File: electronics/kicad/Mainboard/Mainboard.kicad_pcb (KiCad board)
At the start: 2 copper layers, 99 x 53 mm, 30 parts, among them J1 GND Pair, J10 Conn_01x05, J11 Box Switch 1, J12 Box Switch 2, J13 Bos Switch 3, J14 LED Strip, J2 X-Axis Hall, J3 Y-Axis Hall, J4 Conn_01x05, J5 Conn_01x05, J6 USB_A_Stacked, J7 Conn_01x05, J8 Conn_01x05, J9 Conn_01x05, M2.5 MountingHole_2.7mm_M2.5_DIN96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, U1 ESP32-C6-DevKitC-1, U2 MCP23017_SP

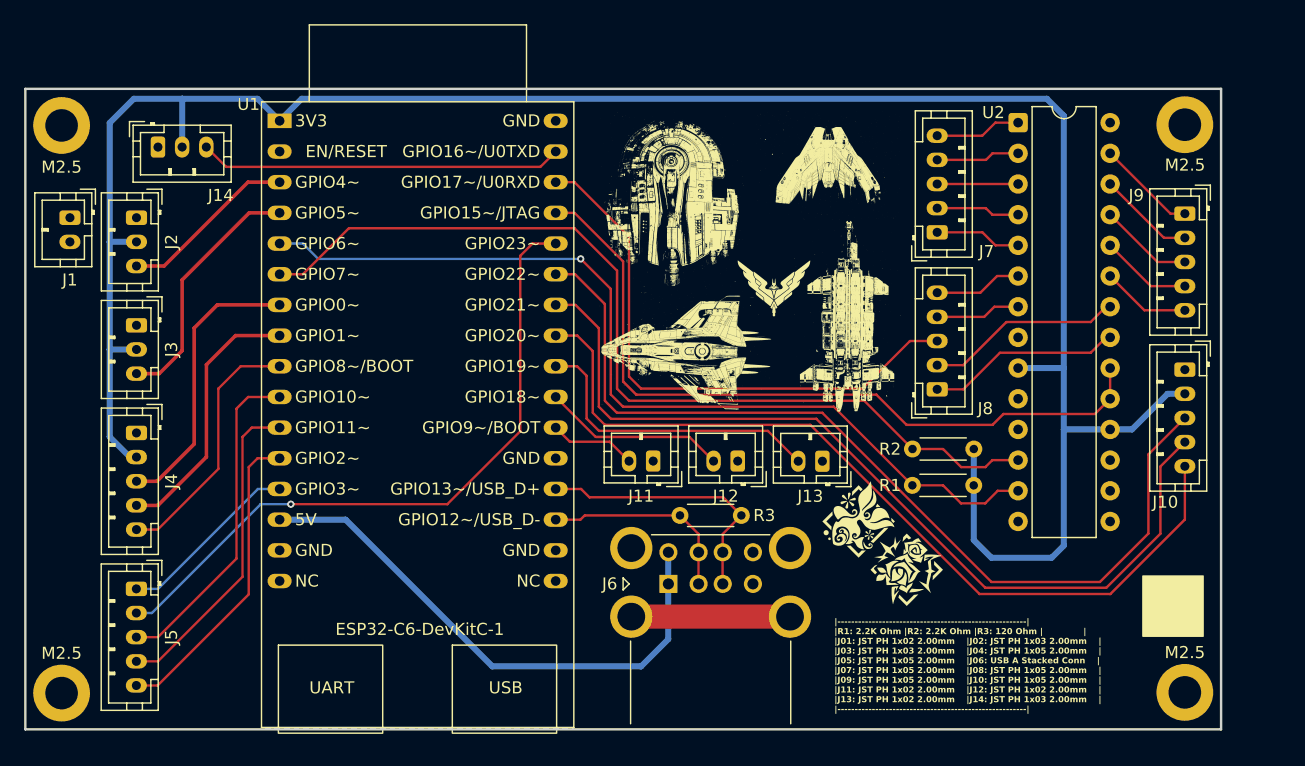
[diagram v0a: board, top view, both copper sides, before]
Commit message: Updated Schematic
Some Parts were replaced with Hand Solder SMD components where possible. Routing changed to work with new parts
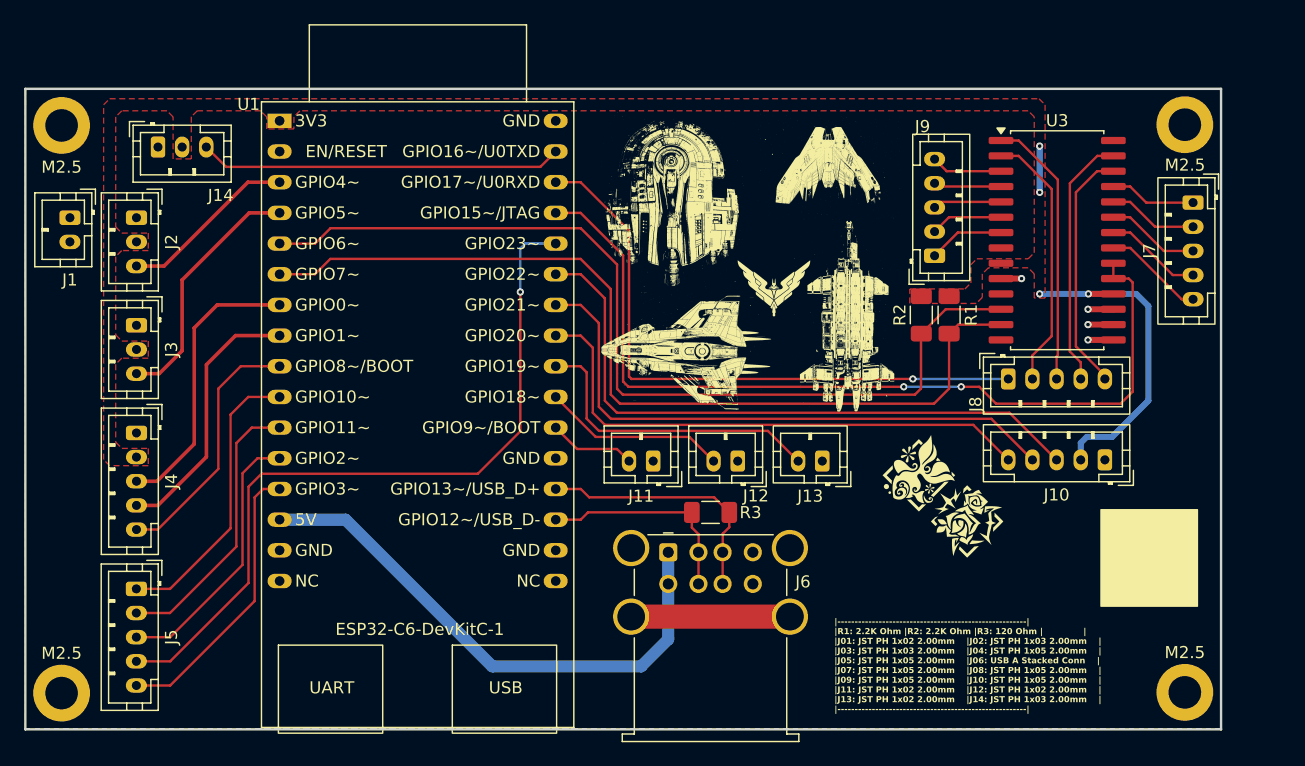
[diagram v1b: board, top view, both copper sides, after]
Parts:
- removed U2: MCP23017_SP, Package_DIP:DIP-28_W7.62mm
- added U3: MCP23017x-x-SO, Package_SO:SOIC-28W_7.5x17.9mm_P1.27mm, F.Cu at (186.4, 84.7)
- J6: footprint Connector_USB:USB_A_CUI_UJ2-ADH-TH_Horizontal_Stacked -> Connector_USB:USB_A_Wuerth_61400826021_Horizontal_Stacked
- R1, R2, R3: footprint Resistor_THT:R_Axial_DIN0204_L3.6mm_D1.6mm_P5.08mm_Horizontal -> Resistor_SMD:R_1206_3216Metric_Pad1.30x1.75mm_HandSolder
- moved J7 21.3 mm to (197.7, 81.6), turned to -90 degrees
- moved J9 21.0 mm to (176.3, 86.0), turned to 90 degrees
- moved R1 14.3 mm to (177.5, 90.9), turned to -90 degrees
- moved R2 11.9 mm to (175.2, 90.9), turned to -90 degrees
- moved J10 9.98 mm to (190.4, 102.9), turned to 180 degrees
- moved G*** 6.40 mm to (179.0, 108.0)
- moved G*** 6.28 mm to (175.0, 104.0)
- moved J8 5.95 mm to (182.4, 96.2), turned to 0 degrees
- moved J6 2.62 mm to (154.2, 110.5), turned to 0 degrees
- moved R3 2.56 mm to (157.8, 107.2)
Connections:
- net Vcc renamed 3V3
- J5 pad 1: Primary Trigger -> Base Button
- J5 pad 2: Secondary Trigger -> Head Button
- J5 pad 3: Base Button -> Face Button
- J5 pad 4: Head Button -> Secondary Trigger
- J5 pad 5: Face Button -> Primary Trigger
- J8 pad 1: Face Hat Right - Center -> Face Hat Right - Down
- J8 pad 3: Face Hat Right - Down -> Face Hat Right - Center
- U1 pad 5: SDA -> SCK
- U1 pad 6: SCK -> SDA
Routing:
- net 3V3: track 185.9 -> 32.1 mm, vias 0 -> 4
- net RE B: track 70.9 -> 44.9 mm
- net RE A: track 73.9 -> 48.8 mm
- net RE Switch: track 76.8 -> 52.8 mm
- net Face Hat Right - Right: track 7.05 -> 21.1 mm
- net Face Hat Right - Up: track 7.27 -> 20.3 mm
- net INT: track 62.4 -> 72.9 mm, vias 0 -> 2
- net Primary Trigger: track 15.3 -> 23.6 mm
- net GND: track 13.2 -> 21.2 mm, vias 0 -> 4
- net Secondary Trigger: track 55.9 -> 62.6 mm
- net Face Hat Right - Center: track 16.1 -> 22.6 mm
- net Face Hat Right - Left: track 16.3 -> 21.7 mm
- net Face Hat Right - Down: track 47.1 -> 51.3 mm, vias 0 -> 1
- net Base Button: track 27.4 -> 24.0 mm
- net Head Button: track 26.7 -> 23.3 mm
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- added copper zone on F.Cu, net 3V3
